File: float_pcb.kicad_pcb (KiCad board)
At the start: 4 copper layers, 64 x 64 mm, 78 parts, among them J1 Batt, J2 Switch, J3 USB_C, J4 I2C, J5 I2C, J6 Conn_01x03, J7 Conn_01x05, J8 Light, Q1 AO3400A, U1 ESP32-S3-WROOM-1U, U2 TPSM863252, U3 TPSM863252

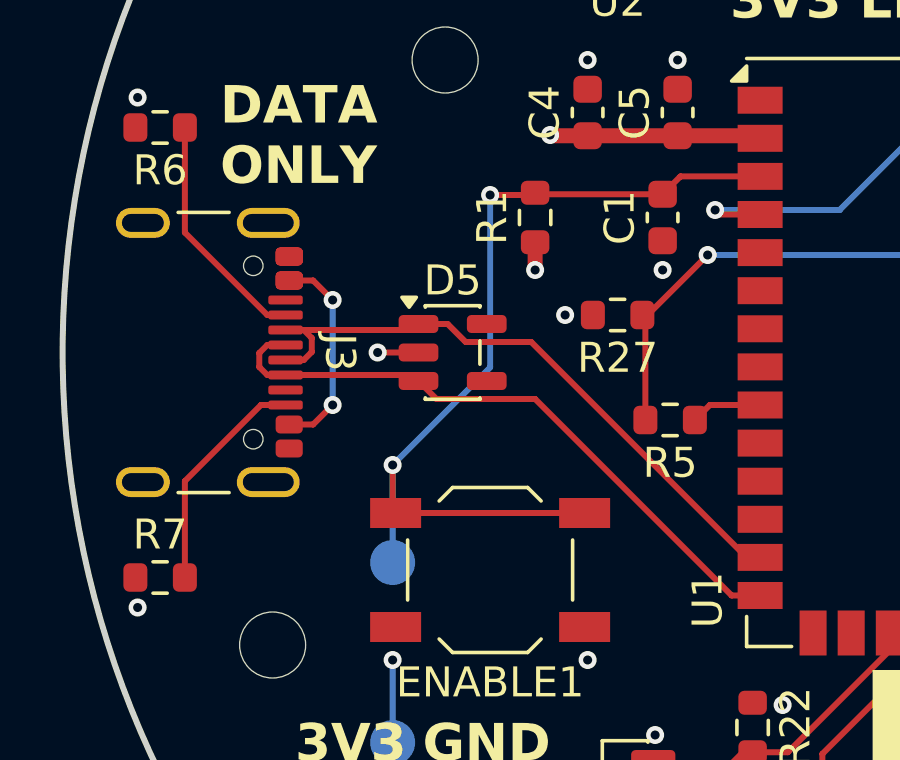
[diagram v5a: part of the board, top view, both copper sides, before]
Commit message: Continuing Test Pads and some placement things
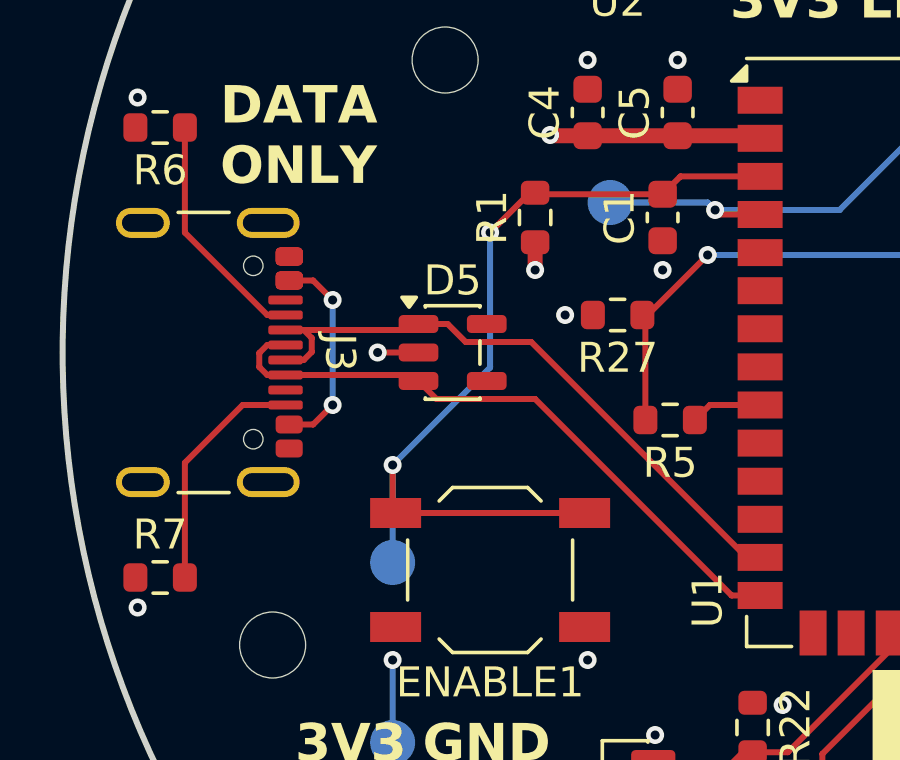
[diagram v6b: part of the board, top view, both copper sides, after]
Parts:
- added TP11: BATT_ADC, TestPoint:TestPoint_Pad_D1.5mm, B.Cu at (134.8, 100.0)
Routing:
- net BATT_SENSE: track 40.1 -> 43.7 mm
- net Net-(U1-EN): track 30.8 -> 30.1 mm
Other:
- board text added: "ADC"

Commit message: V5: Sent for production!
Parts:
- C14: value 470uF -> 470u
- moved H3 14.8 mm to (175.2, 116.5)
- moved C14 1.21 mm to (163.2, 96.0), turned to 180 degrees
- renumbered R7 to R10, R10 to R11, R11 to R12, R12 to R13, R13 to R14, R14 to R15, R15 to R16, R16 to R17, R17 to R18, R18 to R19, R19 to R20, R20 to R21, R21 to R22, R22 to R23, R23 to R24, R24 to R25, R25 to R26, R26 to R27, R27 to R6, R8 to R7, R9 to R8, R6 to R9, TP8 to TP10, TP10 to TP11, TP11 to TP5, TP5 to TP6, TP6 to TP7, TP9 to TP8, TP7 to TP9
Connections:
- C11 pad 1: Net-(U3-VOUT) -> Net-(J6-Pin_2)
- C13 pad 2: Net-(U3-VOUT) -> Net-(J6-Pin_2)
- C14 pad 1: Net-(U3-VOUT) -> Net-(J6-Pin_2)
- C14 pad 2: Net-(J6-Pin_2) -> GND
- R13 pad 2: Net-(U3-VOUT) -> Net-(J6-Pin_2)
- R18 pad 2: Net-(U3-VOUT) -> Net-(J6-Pin_2)
- R20 pad 1: BUZZER -> Net-(LS1-Pad1)
- R20 pad 2: Net-(LS1-Pad1) -> BUZZER
- U3 pad 3: Net-(U3-VOUT) -> Net-(J6-Pin_2)
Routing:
- net Net-(U3-VOUT): track 24.1 -> 0.00 mm
- net Net-(J6-Pin_2): track 15.3 -> 38.0 mm
- net GND: track 10.8 -> 8.06 mm

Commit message: V5: oopsie with extra via
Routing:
- net GND: track 8.06 -> 6.92 mm, vias 35 -> 34
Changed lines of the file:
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@@
-	)
-	(segment
-		(start 165.25 108.3875)
-		(end 165.25 107.25)
-		(width 0.2)
-		(layer "F.Cu")
-		(net "GND")
 	)
 	(segment
@@
 		(net "GND")
 	)
-	(via
-		(at 165.25 107.25)
-		(size 0.6)
-		(drill 0.3)
-		(layers "F.Cu" "B.Cu")
-		(net "GND")
-	)
